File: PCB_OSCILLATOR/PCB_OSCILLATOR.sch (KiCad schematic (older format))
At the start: 35 parts

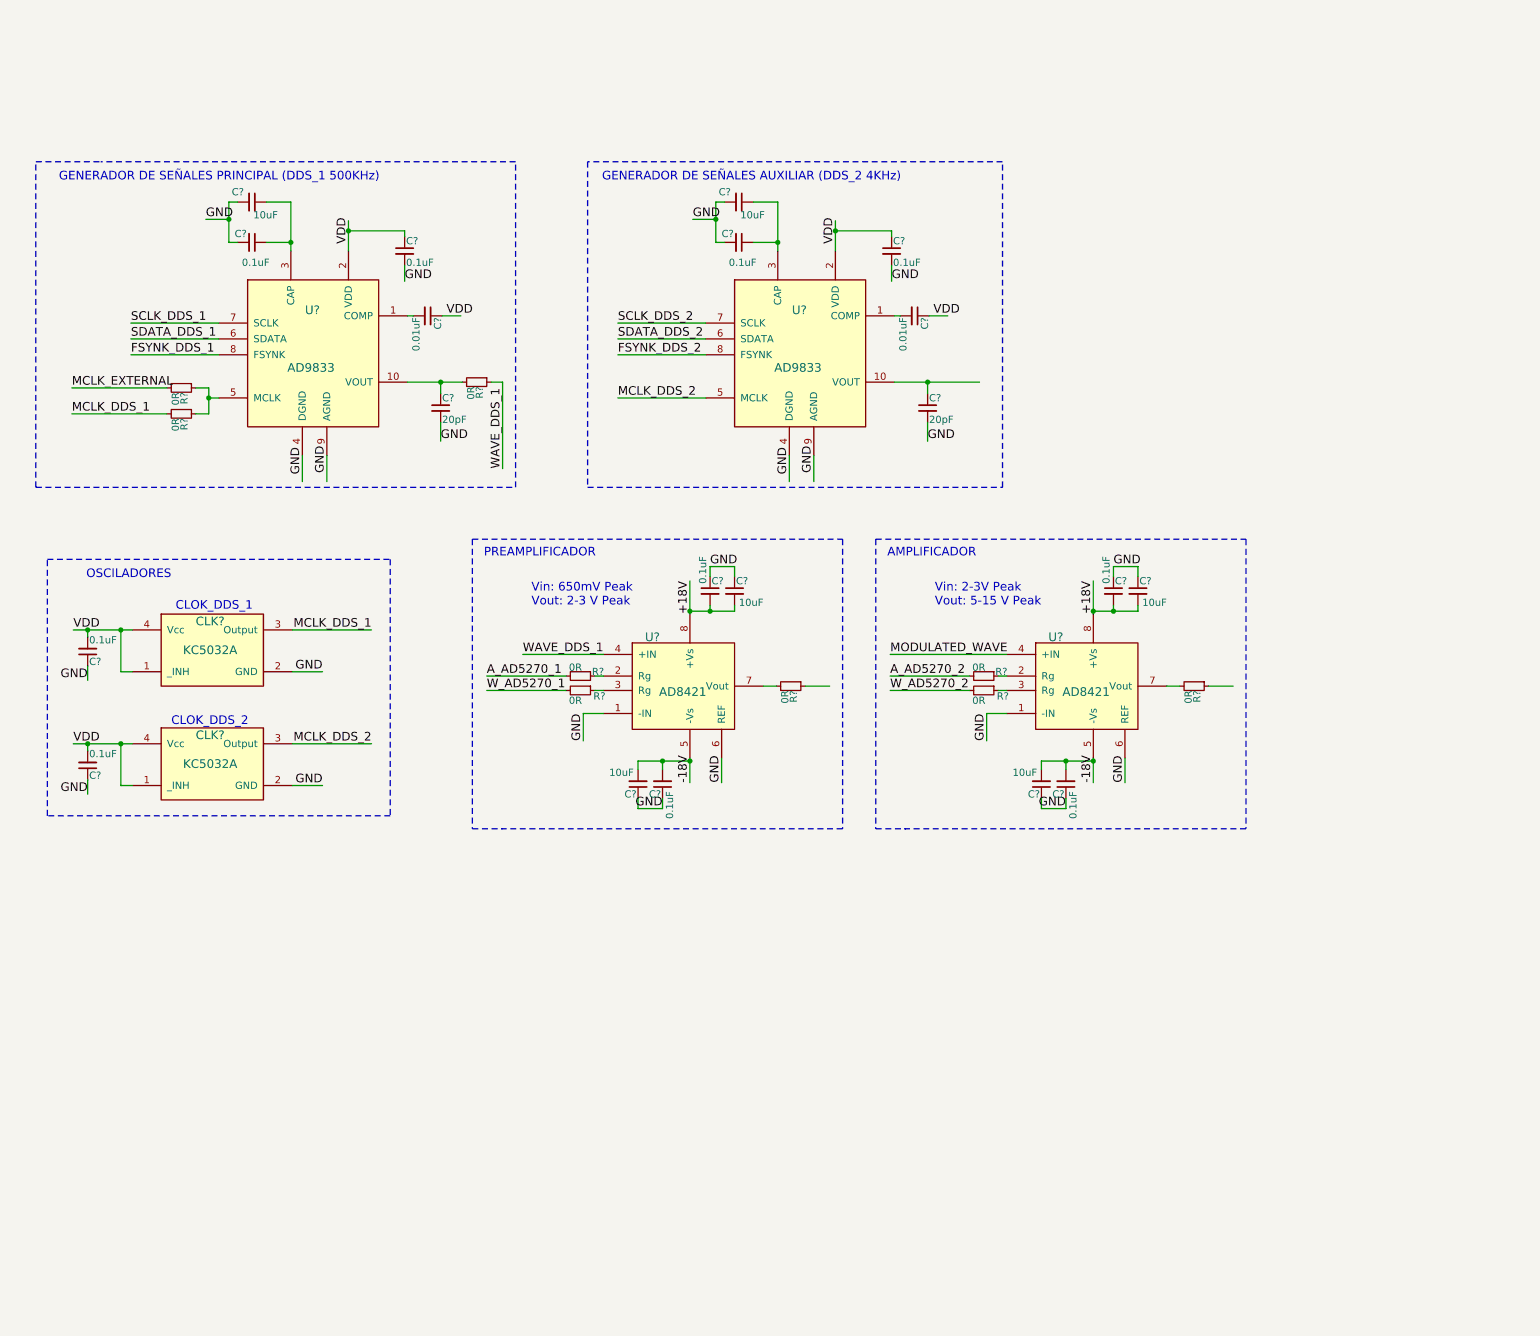
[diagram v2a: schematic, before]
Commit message: Incluyo el ADG849
Nombro algunas señales adicionales
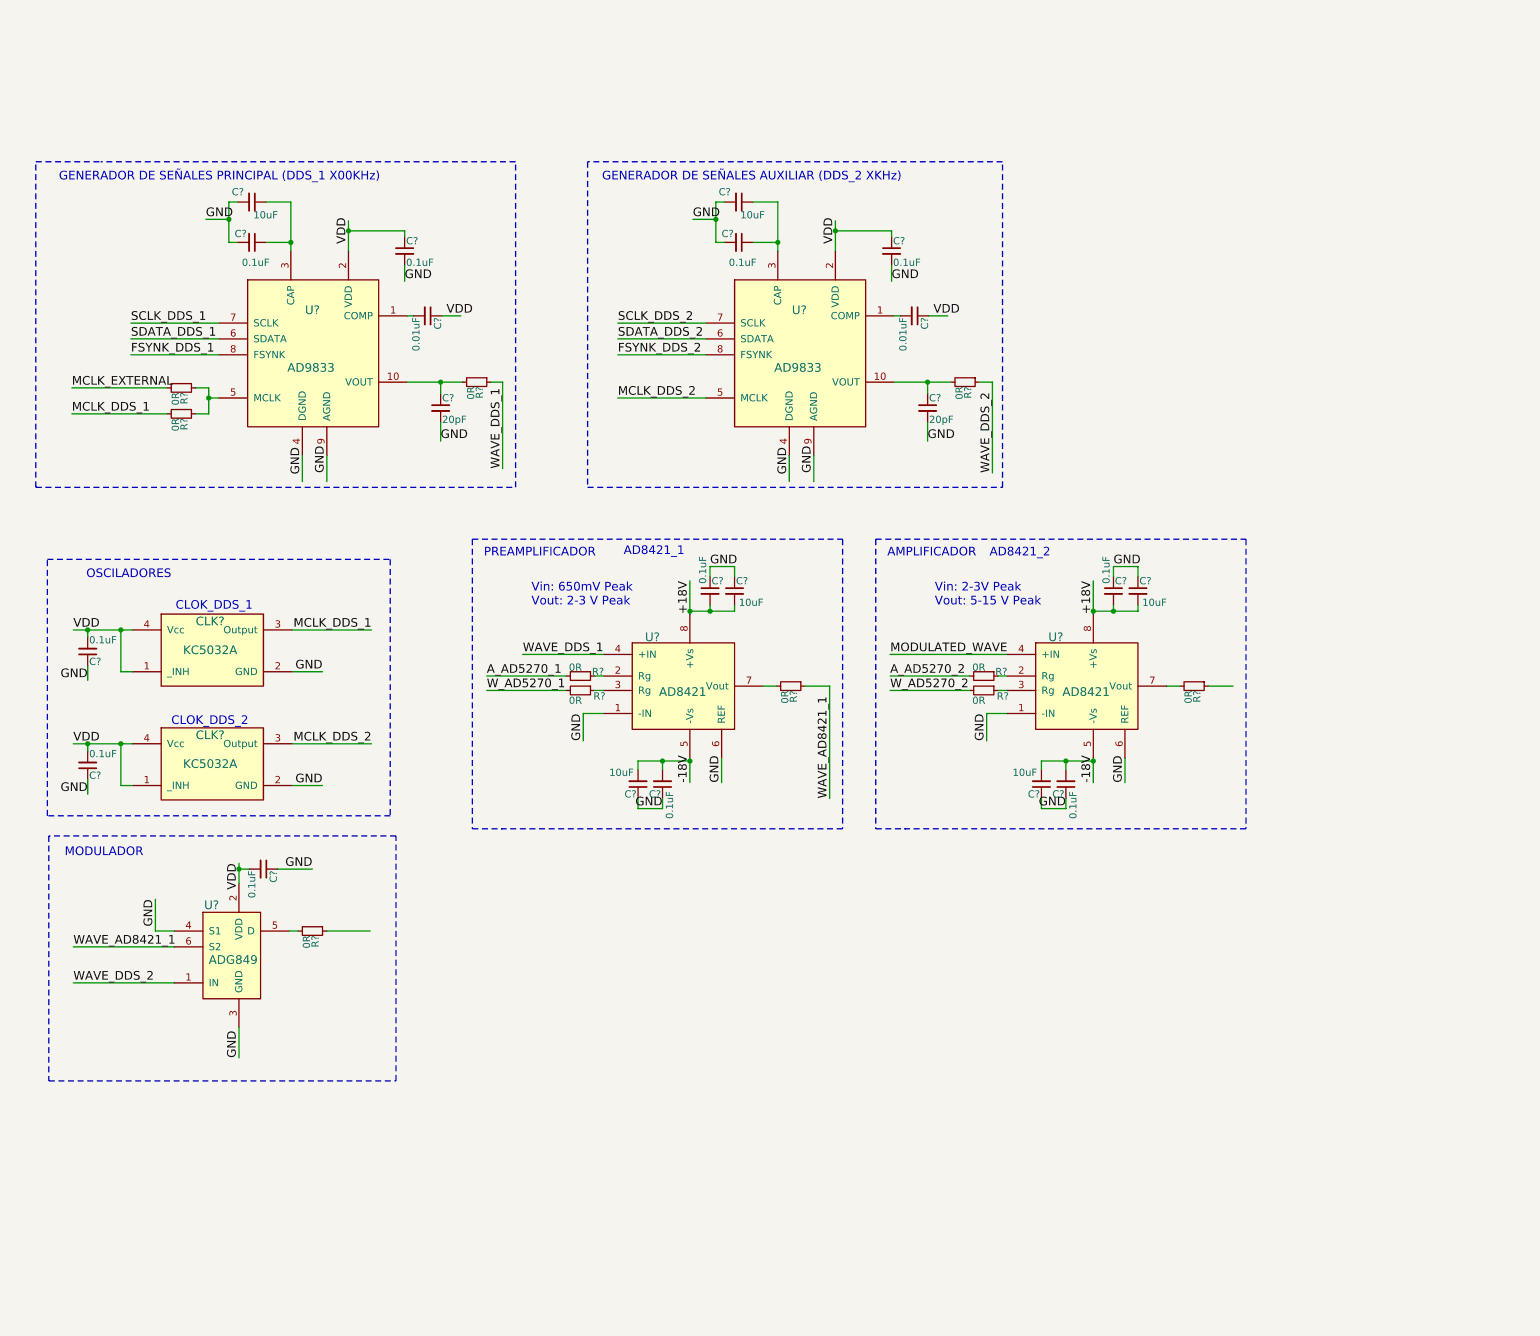
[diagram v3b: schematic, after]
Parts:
- added C?: 0.1uF, symbol C_Small
- added R? (x2): 0R, symbol R_Small
- added U?: ADG849, symbol ADG849
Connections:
- net labels added: WAVE_AD8421_1, WAVE_DDS_2
- wire segments 113 -> 126
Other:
- note added: "AD8421_1"
- note added: "AD8421_2"
- note added: "GENERADOR DE SEÑALES AUXILIAR (DDS_2 XKHz)\n"
- note added: "GENERADOR DE SEÑALES PRINCIPAL (DDS_1 X00KHz)\n"
- note added: "MODULADOR"
- note removed: "GENERADOR DE SEÑALES AUXILIAR (DDS_2 4KHz)\n"
- note removed: "GENERADOR DE SEÑALES PRINCIPAL (DDS_1 500KHz)\n"
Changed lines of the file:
@@
 GND
 Text Notes 1010 1220 0    60   ~ 0
-GENERADOR DE SEÑALES PRINCIPAL (DDS_1 500KHz)\n
+GENERADOR DE SEÑALES PRINCIPAL (DDS_1 X00KHz)\n
 $Comp
 L AD9833 U?
@@
 GND
 Text Notes 4780 1220 0    60   ~ 0
-GENERADOR DE SEÑALES AUXILIAR (DDS_2 4KHz)\n
+GENERADOR DE SEÑALES AUXILIAR (DDS_2 XKHz)\n
 $Comp
 L KC5032A CLK?
@@
 Connection ~ 5570 1480
 Wire Wire Line
-	6810 2610 7400 2610
-Wire Wire Line
 	7040 2690 7040 2610
 Connection ~ 7040 2610
@@
 Wire Notes Line
 	6680 3700 6680 5710
+$Comp
+L ADG849 U?
+U 1 1 590F8A79
+P 2210 6620
+F 0 "U?" H 2070 7000 60  0000 C CNN
+F 1 "ADG849" H 2220 6620 60  0000 C CNN
+F 2 "" H 2210 6620 60  0000 C CNN
+F 3 "" H 2210 6620 60  0000 C CNN
+	1    2210 6620
+	1    0    0    -1
+$EndComp
+Wire Wire Line
+	2260 6090 2260 5950
+Wire Wire Line
+	2260 7090 2260 7300
+$Comp
+L R_Small R?
+U 1 1 590FBD26
+P 2770 6420
+F 0 "R?" H 2800 6440 50  0000 L CNN
+F 1 "0R" H 2800 6380 50  0000 L CNN
+F 2 "" H 2770 6420 50  0000 C CNN
+F 3 "" H 2770 6420 50  0000 C CNN
+	1    2770 6420
+	0    1    1    0
+$EndComp
+Wire Wire Line
+	2670 6420 2610 6420
+Wire Wire Line
+	2870 6420 3170 6420
+Wire Wire Line
+	1110 6530 1810 6530
+Wire Wire Line
+	1110 6780 1810 6780
+Text Label 1680 6200 3    60   ~ 0
+GND
+Wire Wire Line
+	6360 4720 6360 5500
+Text Notes 4930 3820 0    60   ~ 0
+AD8421_1
+Text Notes 7470 3830 0    60   ~ 0
+AD8421_2
+Text Label 6360 5500 1    60   ~ 0
+WAVE_AD8421_1
+Text Label 1110 6530 0    60   ~ 0
+WAVE_AD8421_1
+Wire Wire Line
+	1810 6420 1680 6420
+Wire Wire Line
+	1680 6420 1680 6200
+$Comp
+L R_Small R?
+U 1 1 591096B6
+P 7300 2610
+F 0 "R?" H 7330 2630 50  0000 L CNN
+F 1 "0R" H 7330 2570 50  0000 L CNN
+F 2 "" H 7300 2610 50  0000 C CNN
+F 3 "" H 7300 2610 50  0000 C CNN
+	1    7300 2610
+	0    1    1    0
+$EndComp
+Wire Wire Line
+	6810 2610 7200 2610
+Wire Wire Line
+	7400 2610 7490 2610
+Wire Wire Line
+	7490 2610 7490 3240
+Text Label 7490 3240 1    60   ~ 0
+WAVE_DDS_2
+Text Label 1110 6780 0    60   ~ 0
+WAVE_DDS_2
+Text Label 2260 7300 1    60   ~ 0
+GND
+Text Label 2260 5950 3    60   ~ 0
+VDD
+$Comp
+L C_Small C?
+U 1 1 5910E61A
+P 2430 5990
+F 0 "C?" H 2440 6060 50  0000 L CNN
+F 1 "0.1uF" H 2440 5910 50  0000 L CNN
+F 2 "" H 2430 5990 50  0000 C CNN
+F 3 "" H 2430 5990 50  0000 C CNN
+	1    2430 5990
+	0    1    1    0
+$EndComp
+Wire Wire Line
+	2330 5990 2260 5990
+Connection ~ 2260 5990
+Wire Wire Line
+	2530 5990 2770 5990
+Text Label 2770 5990 2    60   ~ 0
+GND
+Wire Notes Line
+	940  5760 940  7460
+Wire Notes Line
+	940  7460 3350 7460
+Wire Notes Line
+	3350 7460 3350 5760
+Wire Notes Line
+	3350 5760 940  5760
+Text Notes 1050 5910 0    60   ~ 0
+MODULADOR
 $EndSCHEMATC

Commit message: Esquematico casi final
faltan agregar los leds que indiquen presencia de alimentación
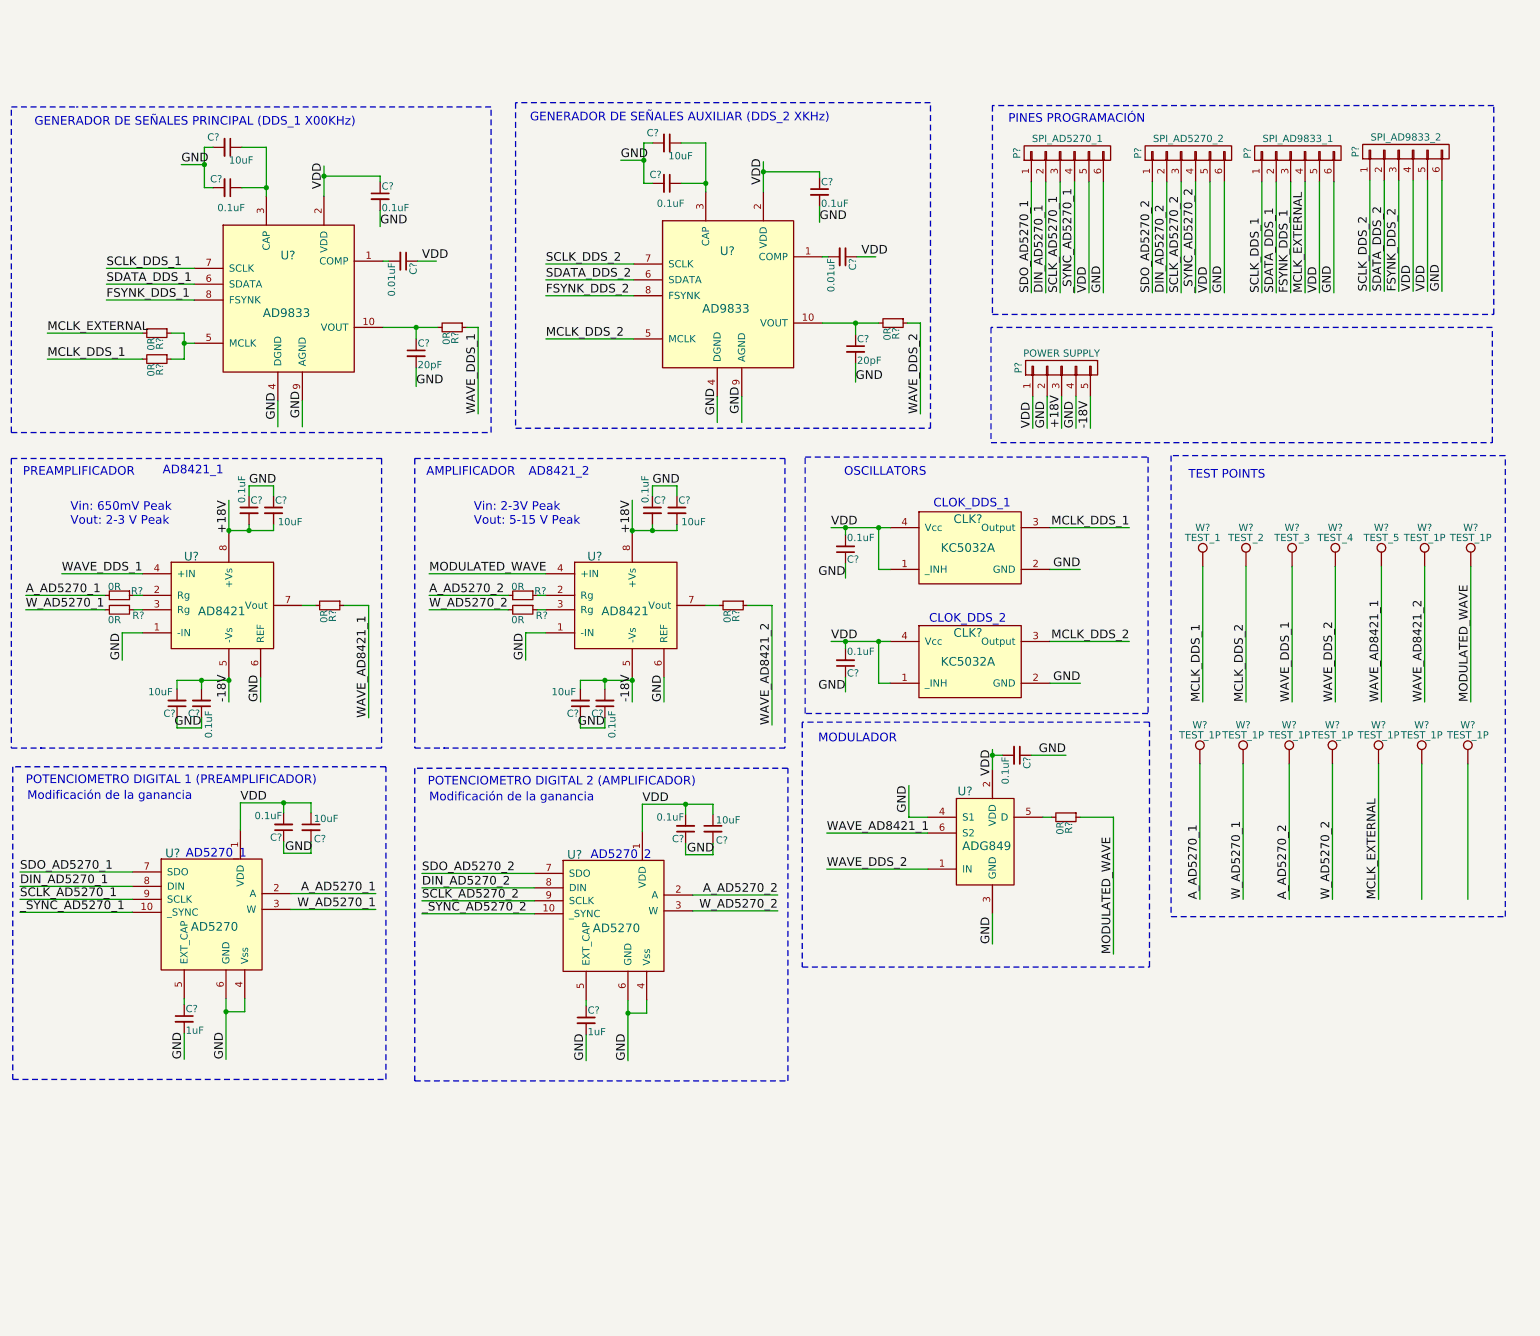
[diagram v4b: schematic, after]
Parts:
- added C? (x2): 1uF, symbol C_Small
- added C? (x2): 0.1uF, symbol C_Small
- added C? (x2): 10uF, symbol C_Small
- added P?: SPI_AD5270_1, symbol CONN_01X06
- added P?: SPI_AD5270_2, symbol CONN_01X06
- added P?: SPI_AD9833_1, symbol CONN_01X06
- added P?: SPI_AD9833_2, symbol CONN_01X06
- added P?: POWER SUPPLY, symbol CONN_01X05
- added U? (x2): AD5270, symbol AD5270
- added W?: TEST_1, symbol TEST_1P
- added W?: TEST_2, symbol TEST_1P
- added W?: TEST_3, symbol TEST_1P
- added W?: TEST_4, symbol TEST_1P
- added W?: TEST_5, symbol TEST_1P
- added W? (x9): TEST_1P, symbol TEST_1P
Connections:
- net labels added: DIN_AD5270_1, DIN_AD5270_2, SCLK_AD5270_1, SCLK_AD5270_2, SDO_AD5270_1, SDO_AD5270_2, WAVE_AD8421_2, _SYNC_AD5270_1, _SYNC_AD5270_2
- wire segments 126 -> 207
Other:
- note added: "AD5270_1"
- note added: "AD5270_2"
- note added: "Modificación de la ganancia"
- note added: "OSCILLATORS"
- note added: "PINES PROGRAMACIÓN"
- note added: "POTENCIOMETRO DIGITAL 1 (PREAMPLIFICADOR)"
- note added: "POTENCIOMETRO DIGITAL 2 (AMPLIFICADOR)"
- note added: "TEST POINTS"
- note removed: "OSCILADORES"
- moved on the sheet: C?, CLK?, R?, U?

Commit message: Esquematico completo
Primera versión de todo el esquematico, falta revisión del grupo
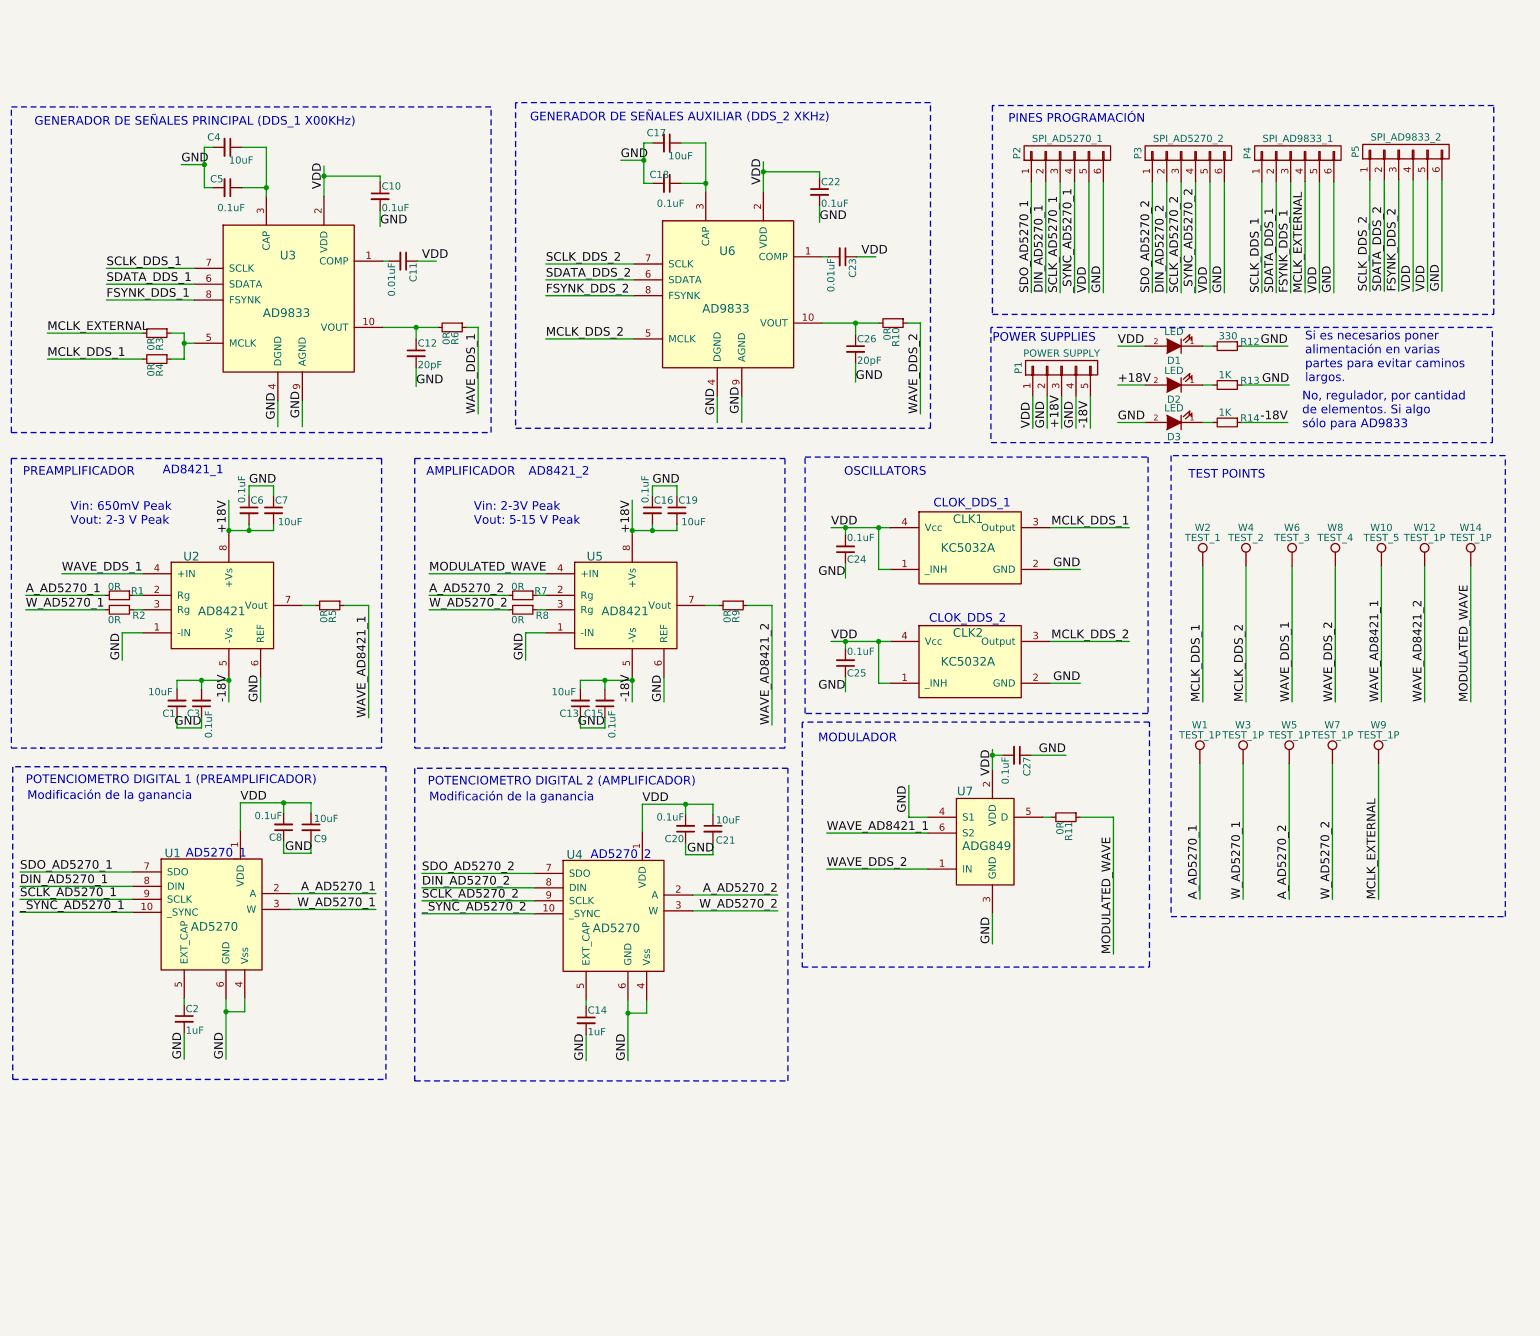
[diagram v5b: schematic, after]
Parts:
- removed W? (x2): TEST_1P, symbol TEST_1P
- added D1, D2, D3: LED, symbol LED
- added R12: 330, symbol R_Small
- added R13, R14: 1K, symbol R_Small
- gave numbers to parts that had none: 64
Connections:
- wire segments 207 -> 214
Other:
- note added: "No, regulador, por cantidad \nde elementos. Si algo \nsólo para AD9833"
- note added: "POWER SUPPLIES"
- note added: "Si es necesarios poner \nalimentación en varias \npartes para evitar caminos\nlargos."
